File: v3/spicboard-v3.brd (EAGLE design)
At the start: 100 x 80 mm, 39 parts, among them IC1 74HC595N, Q1 BC557, Q2 BC557

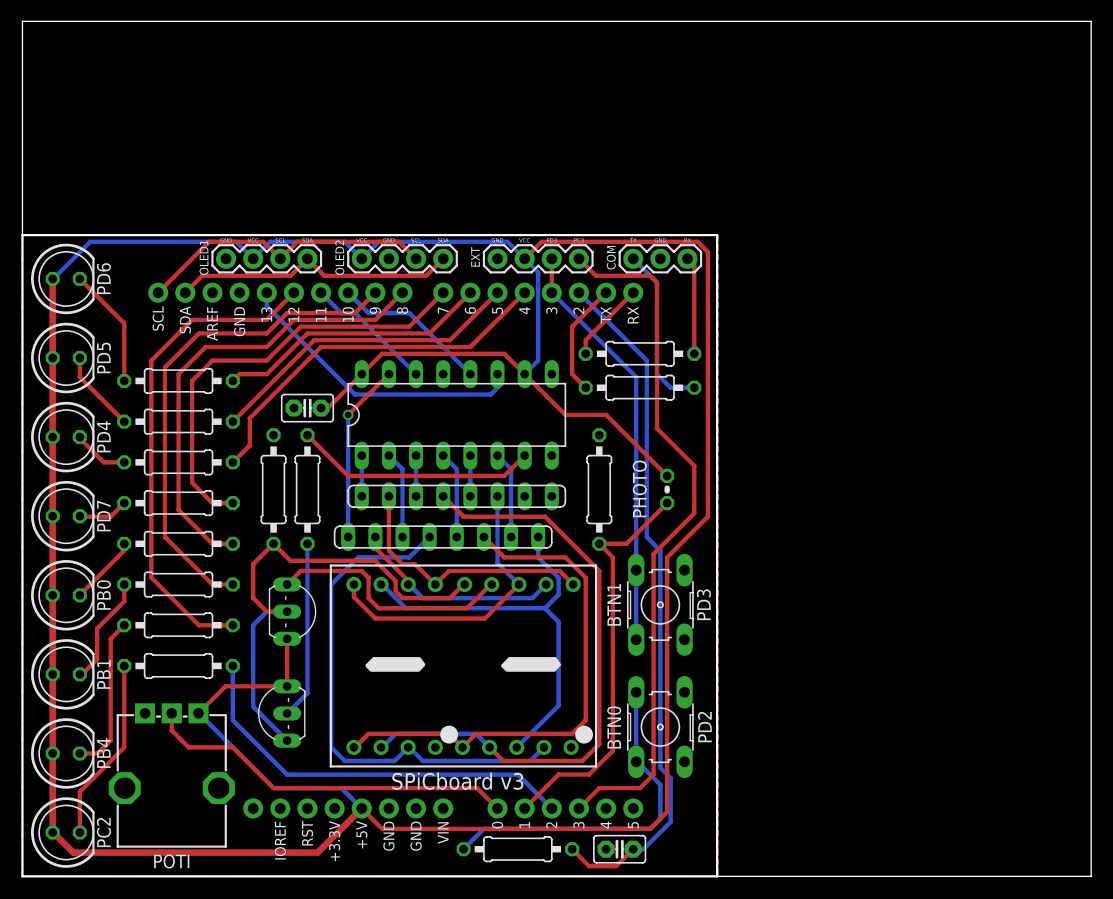
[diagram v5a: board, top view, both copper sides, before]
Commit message: SPiCboard: GND plane
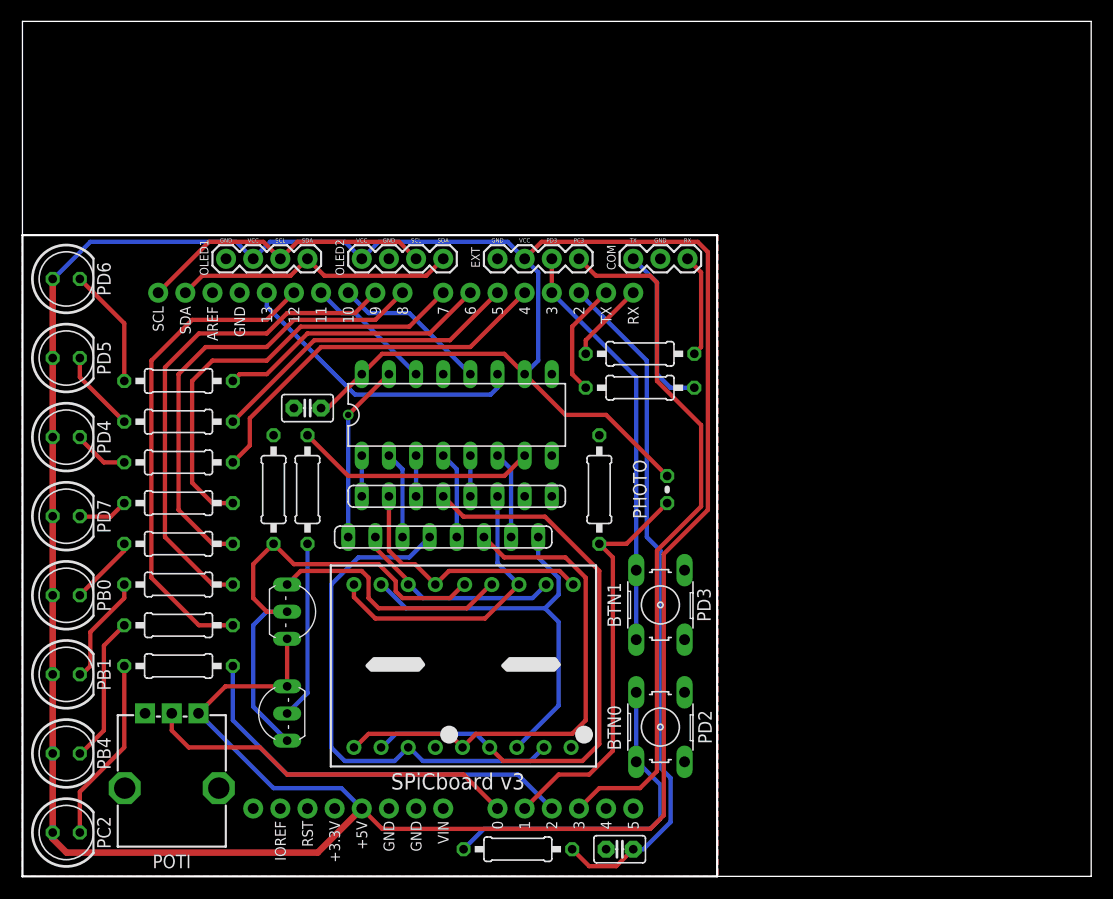
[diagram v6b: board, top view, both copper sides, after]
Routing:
- net N$8: track 14.7 -> 13.8 mm
- net N$21: track 9.15 -> 9.68 mm
- net EXTADC: track 65.6 -> 66.1 mm
- net VCC: track 318.1 -> 318.6 mm
- added copper zone on layer 16, net GND
- removed copper zone on layer 16, net N$22
